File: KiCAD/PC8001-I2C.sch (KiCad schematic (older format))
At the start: 44 parts, among them J1 ADDR-JP, J2 I2C RTC DS3231, J3 I2C OUT, J4 PC8001 Ext Con, J5 I2C ExtOUT1, J6 I2C ExtOUT1, J7 I2C ExtOUT1, J8 I2C ExtOUT1, Q1 2N7000, U1 74HC138, U2 DS1307+, U3 8255, U4 24LC1025, U5 24LC1025, U6 74HC07, U7 74HC4051, U8 74LS32, Y1 32.768kHz

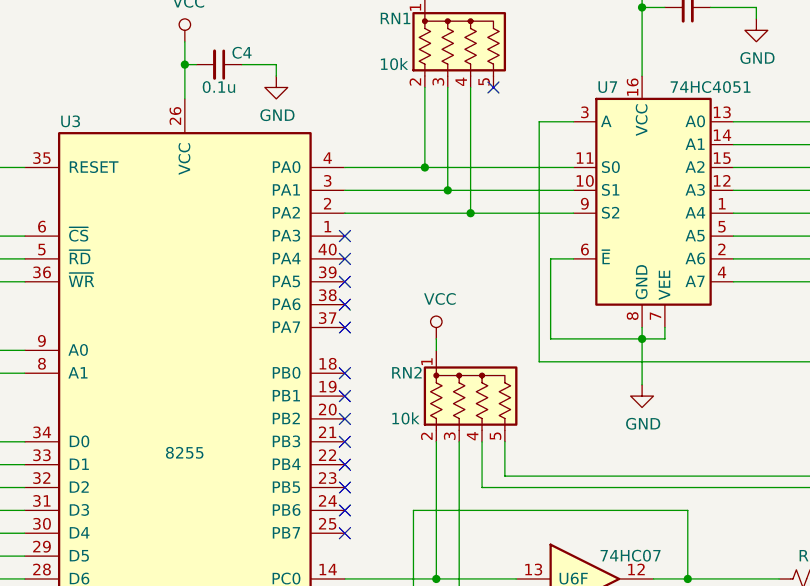
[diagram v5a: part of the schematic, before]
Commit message: サンプルソースをREV1/REV2に分けた
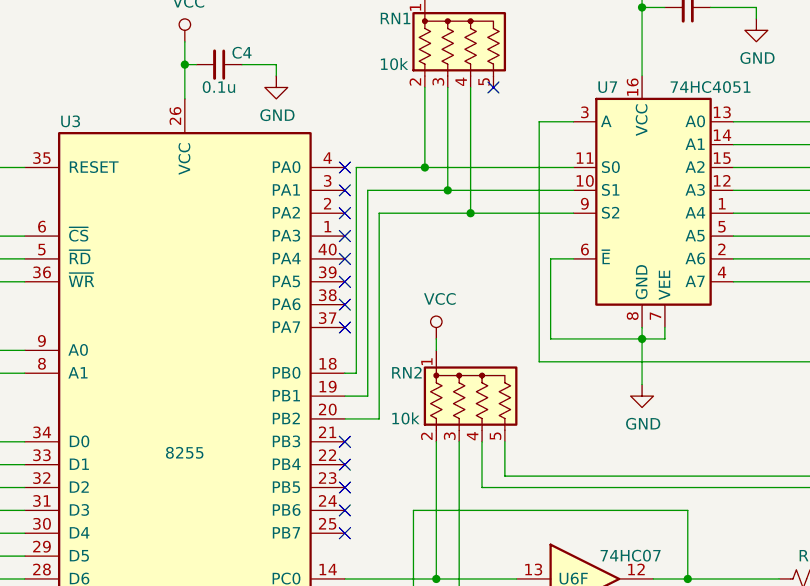
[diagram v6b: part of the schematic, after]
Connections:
- net at U3.18 (PB0): now also RN1.2 (R1), U7.11 (S0)
- net at U3.19 (PB1): now also RN1.3 (R2), U7.10 (S1)
- net at RN1.4 (R3), U7.9 (S2): now also U3.20 (PB2); no longer U3.2 (PA2)
- now unconnected: U3.3 (PA1), U3.4 (PA0)
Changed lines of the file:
@@
 Wire Wire Line
 	2450 3550 2000 3550
-NoConn ~ 5400 2500
-NoConn ~ 5400 2600
-NoConn ~ 5400 2700
 NoConn ~ 5400 2800
 $Comp
@@
 	8250 3800 8700 3800
 Wire Wire Line
-	5400 1600 5750 1600
-Wire Wire Line
 	6400 1700 5850 1700
-Wire Wire Line
-	5400 1800 5950 1800
 NoConn ~ 5400 1900
 NoConn ~ 5400 2300
@@
 Wire Wire Line
 	5750 1250 5750 1600
-Connection ~ 5750 1600
 Wire Wire Line
 	5750 1600 6400 1600
 Wire Wire Line
 	5850 1250 5850 1700
-Connection ~ 5850 1700
-Wire Wire Line
-	5850 1700 5400 1700
 Wire Wire Line
 	5950 1250 5950 1800
-Connection ~ 5950 1800
 Wire Wire Line
 	5950 1800 6400 1800
@@
 NoConn ~ 9650 1750
 NoConn ~ 9650 2100
+NoConn ~ 5400 1600
+NoConn ~ 5400 1700
+NoConn ~ 5400 1800
+Wire Wire Line
+	5400 2500 5450 2500
+Wire Wire Line
+	5450 2500 5450 1600
+Wire Wire Line
+	5450 1600 5750 1600
+Connection ~ 5750 1600
+Wire Wire Line
+	5850 1700 5500 1700
+Wire Wire Line
+	5500 1700 5500 2600
+Wire Wire Line
+	5500 2600 5400 2600
+Connection ~ 5850 1700
+Wire Wire Line
+	5400 2700 5550 2700
+Wire Wire Line
+	5550 2700 5550 1800
+Wire Wire Line
+	5550 1800 5950 1800
+Connection ~ 5950 1800
 $EndSCHEMATC
